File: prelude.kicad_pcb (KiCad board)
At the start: 2 copper layers, 80 x 60 mm, 35 parts, among them J1 CONN_01X50, J2 USB_C, J3 CONN_01X04, J4 CONN_01X08, SW1 SW_Push, U1 LM3671MF-3.3, U2 STM32F411RETx, U3 AP5724, Y1 16MHz

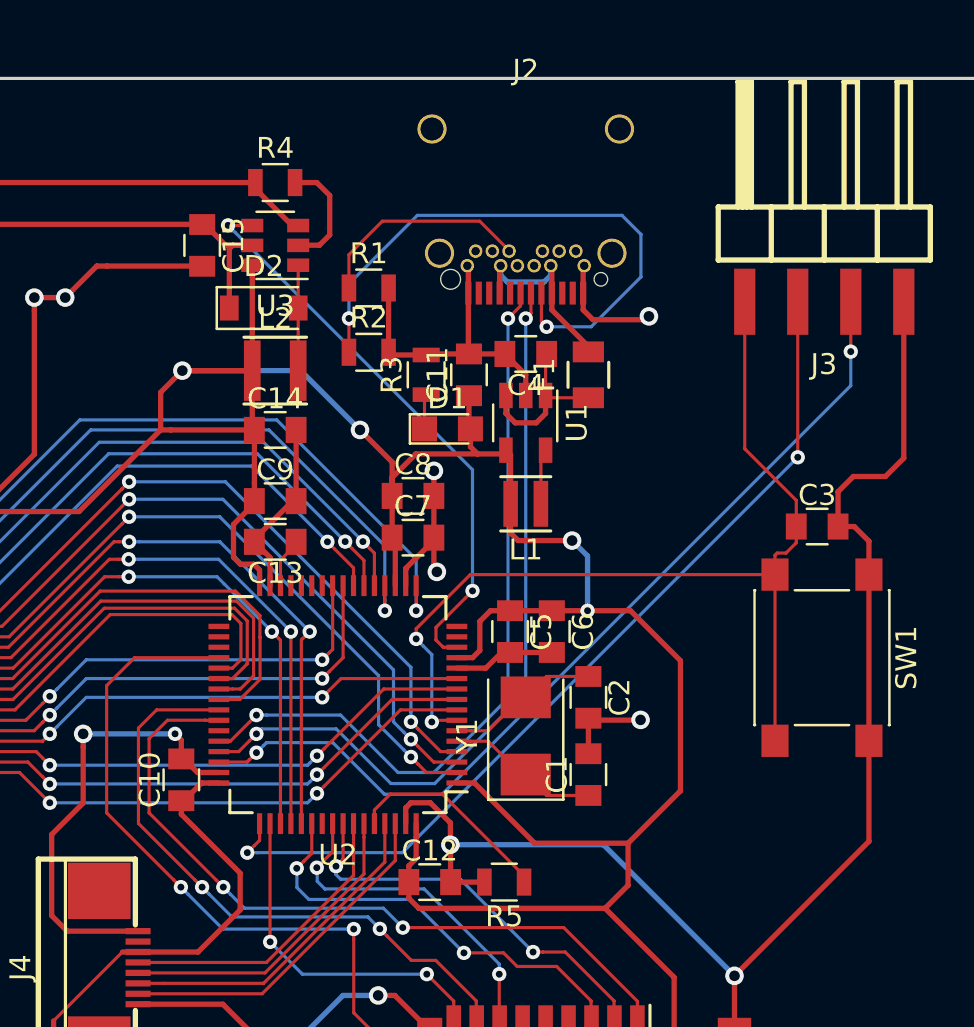
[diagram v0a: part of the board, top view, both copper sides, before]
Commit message: Updates to prelude.kicad_pcb
Reloaded updated netlist, exchanged footprints, adjusted J2 connector and rerouted USB-C portion.
Adds R6, which had not been imported before (by mistake)
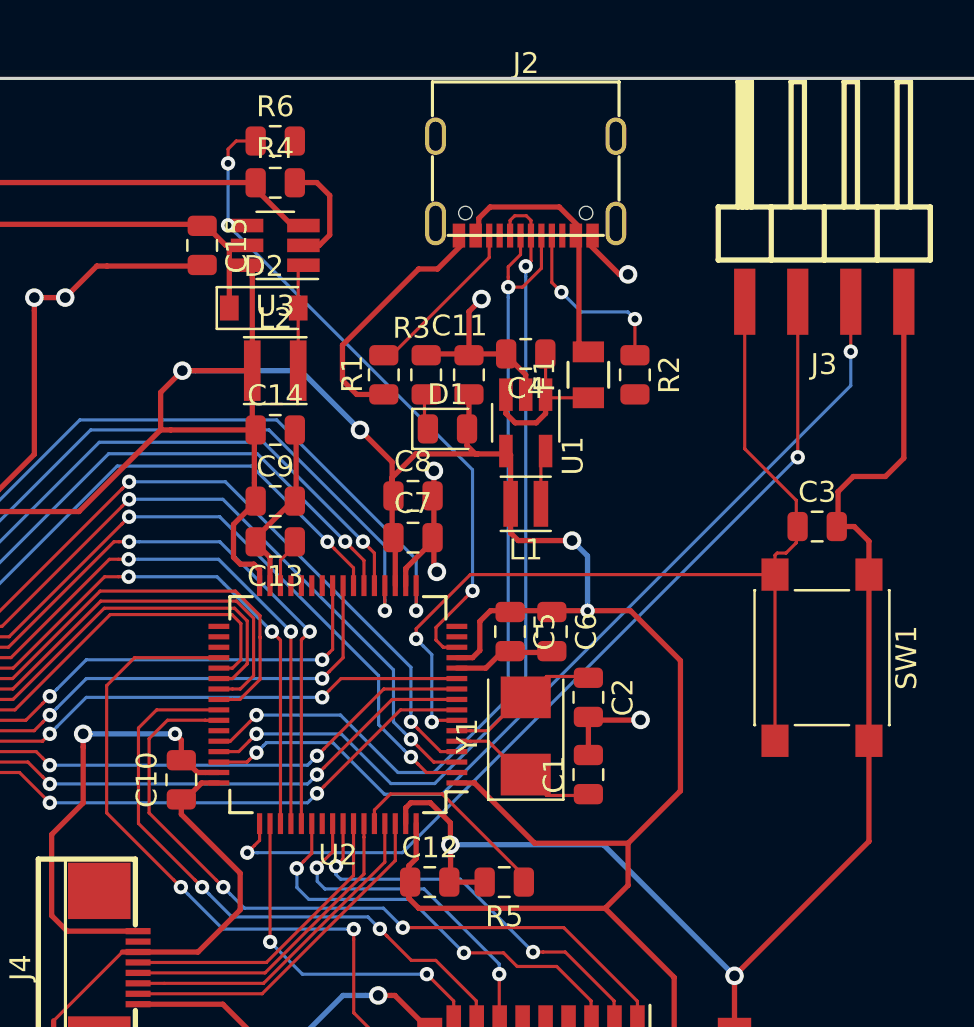
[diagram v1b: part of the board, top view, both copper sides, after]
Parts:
- added R6: 10K, Resistor_SMD:R_0805_2012Metric, F.Cu at (163.0, 43.0)
- C1, C10, C11, C12, C13, C14, C15, C2, C3, C4, C5, C6, C7, C8, C9: footprint Capacitors_SMD:C_0805 -> Capacitor_SMD:C_0805_2012Metric
- D1: footprint LEDs:LED_0805 -> LED_SMD:LED_0805_2012Metric
- D2: footprint Diodes_SMD:D_SOD-123 -> Diode_SMD:D_SOD-123
- J2: footprint volium:Amphenol_12401548E4#2A -> volium:D0-9062-005LG
- J3: value CONN_01X04 -> Conn_01x04
- J4: value CONN_01X08 -> Conn_01x08
- L1: footprint Inductors:Inductor_Taiyo-Yuden_NR-24xx -> Inductor_SMD:L_Taiyo-Yuden_NR-24xx
- L2: footprint Inductors:Inductor_Taiyo-Yuden_NR-30xx -> Inductor_SMD:L_Taiyo-Yuden_NR-30xx
- R1, R2, R3, R4, R5: footprint Resistors_SMD:R_0805 -> Resistor_SMD:R_0805_2012Metric
- SW1: footprint Buttons_Switches_SMD:SW_SPST_PTS645 -> Button_Switch_SMD:SW_SPST_PTS645
- U1: footprint TO_SOT_Packages_SMD:TSOT-23-5 -> Package_TO_SOT_SMD:SOT-23-5_HandSoldering
- U2: footprint Housings_QFP:LQFP-64_10x10mm_Pitch0.5mm -> Package_QFP:LQFP-64_10x10mm_P0.5mm
- U3: footprint TO_SOT_Packages_SMD:SOT-23-6 -> Package_TO_SOT_SMD:SOT-23-6_Handsoldering
- XS1: value SD_ebay-uSD-push/push_SMD -> SD_ebay-uSD-push_push_SMD
- Y1: footprint Crystals:Crystal_SMD_5032-2pin_5.0x3.2mm -> Crystal:Crystal_SMD_5032-2Pin_5.0x3.2mm
- moved R2 12.8 mm to (180.2, 54.2), turned to 270 degrees
- moved R1 4.22 mm to (168.2, 54.2), turned to 270 degrees
- moved J2 1.75 mm to (175.0, 43.9)
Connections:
- J1 pad 1: (no net) -> Net-(J1-Pad1)
- J1 pad 10: (no net) -> Net-(J1-Pad10)
- J1 pad 11: (no net) -> Net-(J1-Pad11)
- J1 pad 12: (no net) -> Net-(J1-Pad12)
- J1 pad 13: (no net) -> Net-(J1-Pad13)
- J1 pad 14: (no net) -> Net-(J1-Pad14)
- J1 pad 15: (no net) -> Net-(J1-Pad15)
- J1 pad 16: (no net) -> Net-(J1-Pad16)
- J1 pad 2: (no net) -> Net-(J1-Pad2)
- J1 pad 3: (no net) -> Net-(J1-Pad3)
- J1 pad 33: (no net) -> Net-(J1-Pad33)
- J1 pad 34: (no net) -> Net-(J1-Pad34)
- J1 pad 35: (no net) -> Net-(J1-Pad35)
- J1 pad 36: (no net) -> Net-(J1-Pad36)
- J1 pad 4: (no net) -> Net-(J1-Pad4)
- J1 pad 42: (no net) -> Net-(J1-Pad42)
- J1 pad 43: (no net) -> Net-(J1-Pad43)
- J1 pad 44: (no net) -> Net-(J1-Pad44)
- J1 pad 45: (no net) -> Net-(J1-Pad45)
- J1 pad 46: (no net) -> Net-(J1-Pad46)
- J1 pad 47: (no net) -> Net-(J1-Pad47)
- J1 pad 48: (no net) -> Net-(J1-Pad48)
- J1 pad 9: (no net) -> Net-(J1-Pad9)
- J2 pad A8: (no net) -> Net-(J2-PadA8)
- J2 pad B6: (no net) -> /USB_D+
- J2 pad B7: (no net) -> /USB_D-
- J2 pad B8: (no net) -> Net-(J2-PadB8)
- J4 pad 2: (no net) -> Net-(J4-Pad2)
- U2 pad 15: (no net) -> Net-(U2-Pad15)
- U2 pad 16: (no net) -> Net-(U2-Pad16)
- U2 pad 26: (no net) -> Net-(U2-Pad26)
- U2 pad 27: (no net) -> Net-(U2-Pad27)
- U2 pad 28: (no net) -> Net-(U2-Pad28)
- U2 pad 29: (no net) -> Net-(U2-Pad29)
- U2 pad 33: (no net) -> Net-(U2-Pad33)
- U2 pad 34: (no net) -> Net-(U2-Pad34)
- U2 pad 35: (no net) -> Net-(U2-Pad35)
- U2 pad 43: (no net) -> Net-(U2-Pad43)
- U2 pad 55: (no net) -> Net-(U2-Pad55)
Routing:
- net Net-(J2-PadA5): track 28.3 -> 8.69 mm
- net /USB_D-: track 36.6 -> 42.9 mm
- net /LED_CTRL: track 27.7 -> 33.1 mm, vias 2 -> 3
- net /USB_D+: track 37.3 -> 42.5 mm
- net GND: track 207.6 -> 211.3 mm, vias 12 -> 13
- net /VBUS: track 9.92 -> 13.0 mm
- net Net-(J2-PadB5): track 10.6 -> 8.04 mm

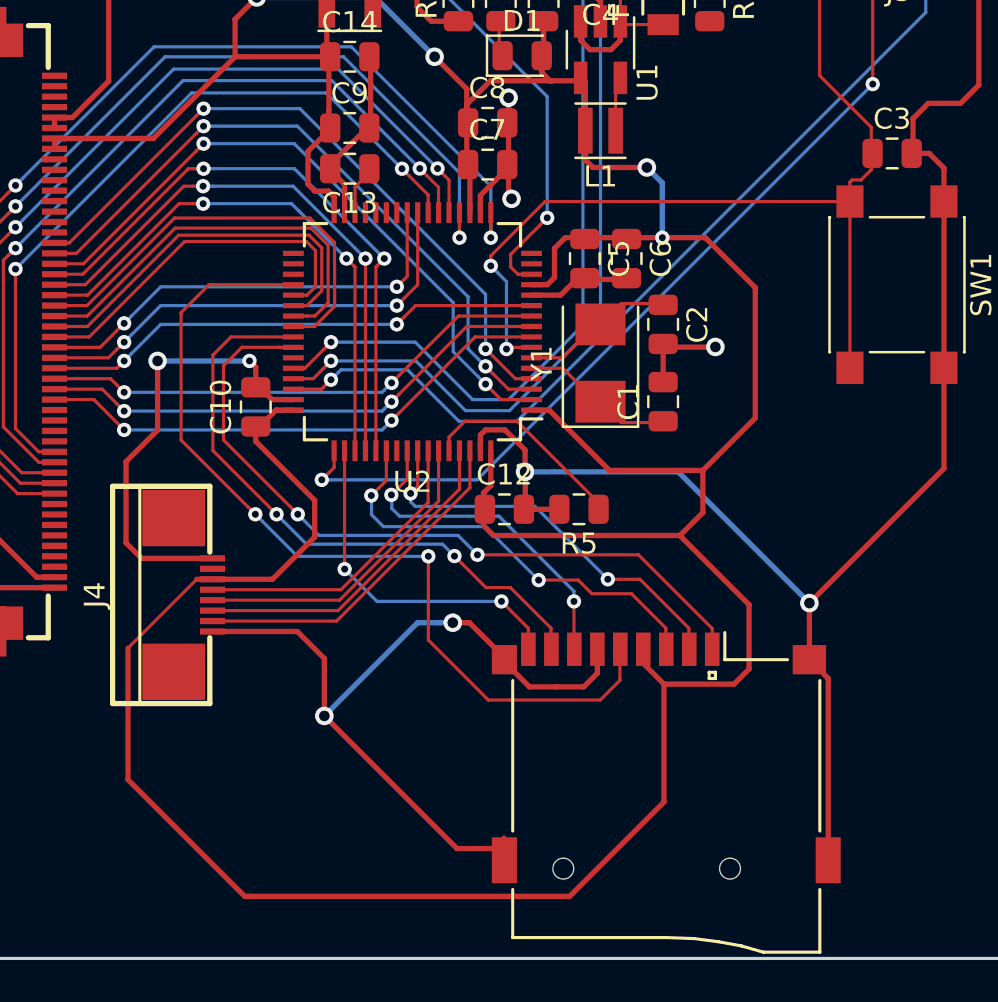
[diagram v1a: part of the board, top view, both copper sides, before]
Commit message: Fixes some routing issues
One pwr track was too narrow
Aligned vias for SDIO signals CMD, D0 and D3
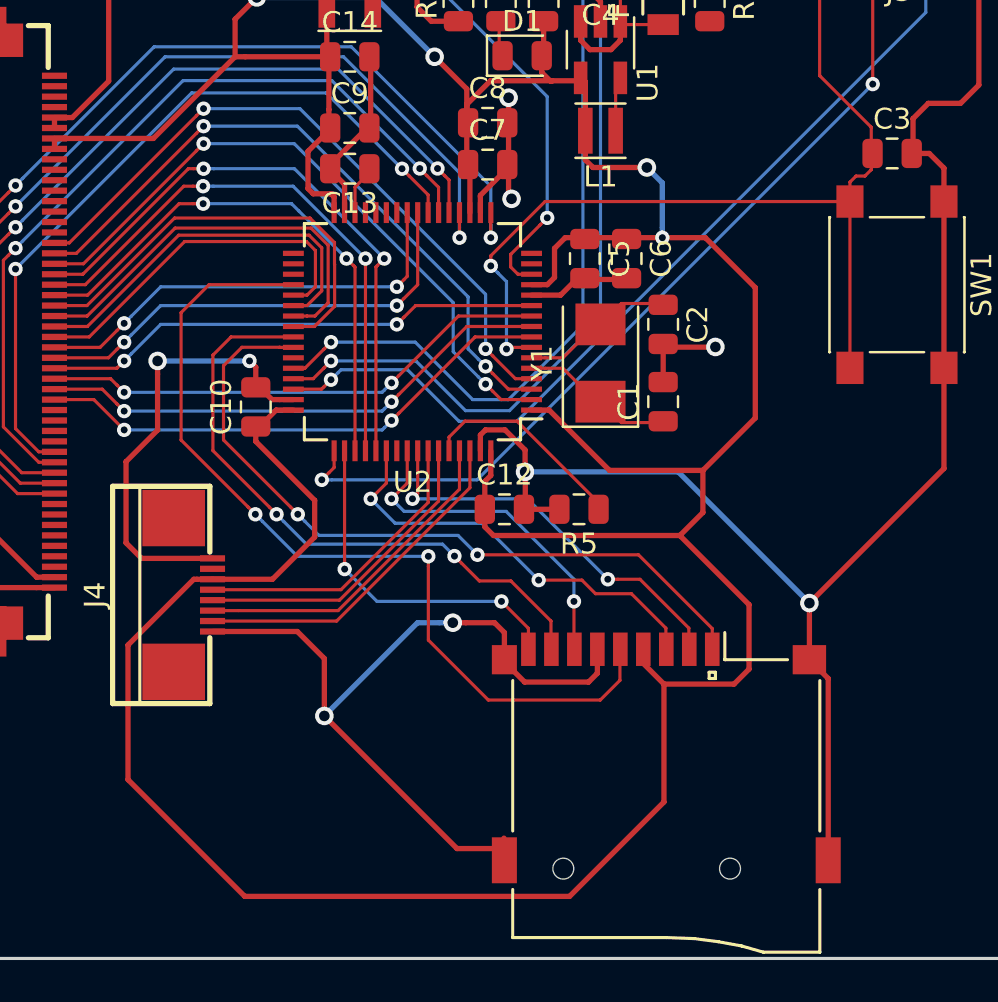
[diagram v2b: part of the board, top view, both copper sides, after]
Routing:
- net GND: track 211.3 -> 211.8 mm

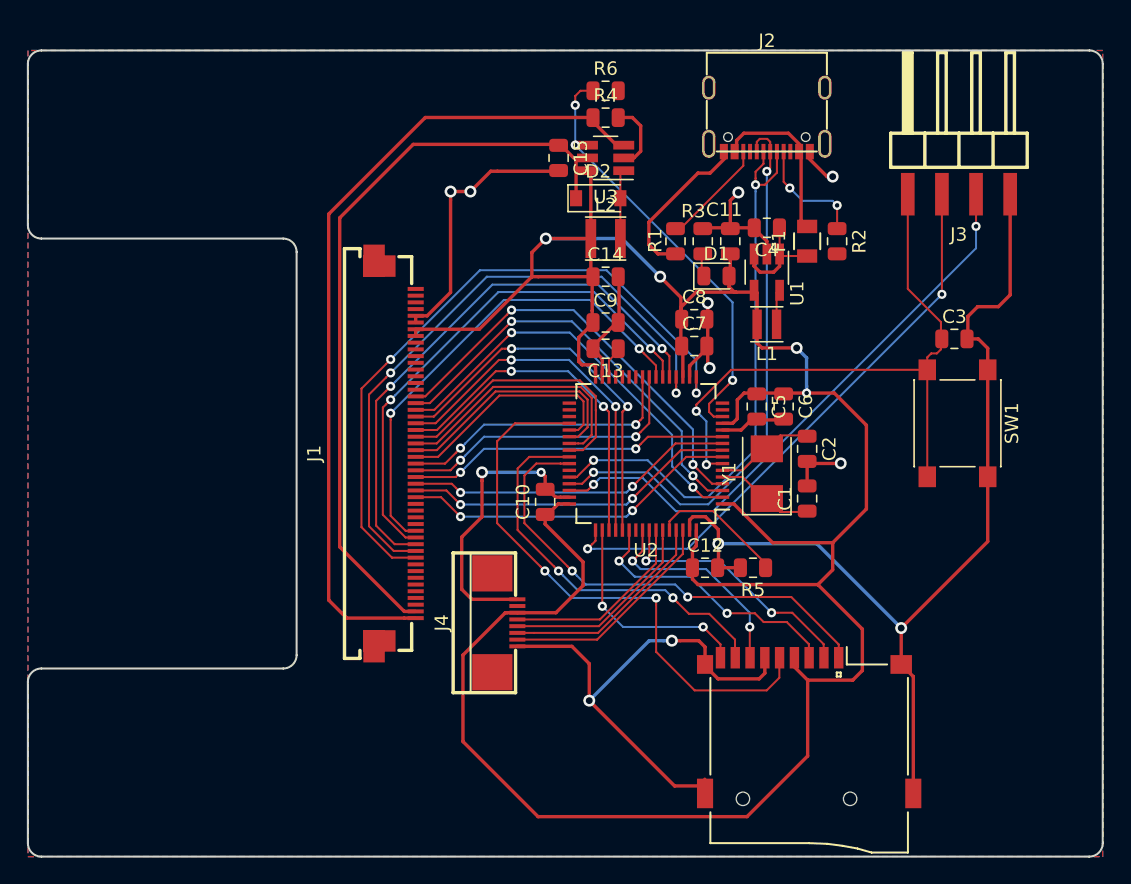
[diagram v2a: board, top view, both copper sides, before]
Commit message: Final touches to prelude
Added via stitching, fixed alignment issues, moved references in silkscreen, added OSH logo and project name and revision
Updates main prelude.pro project file
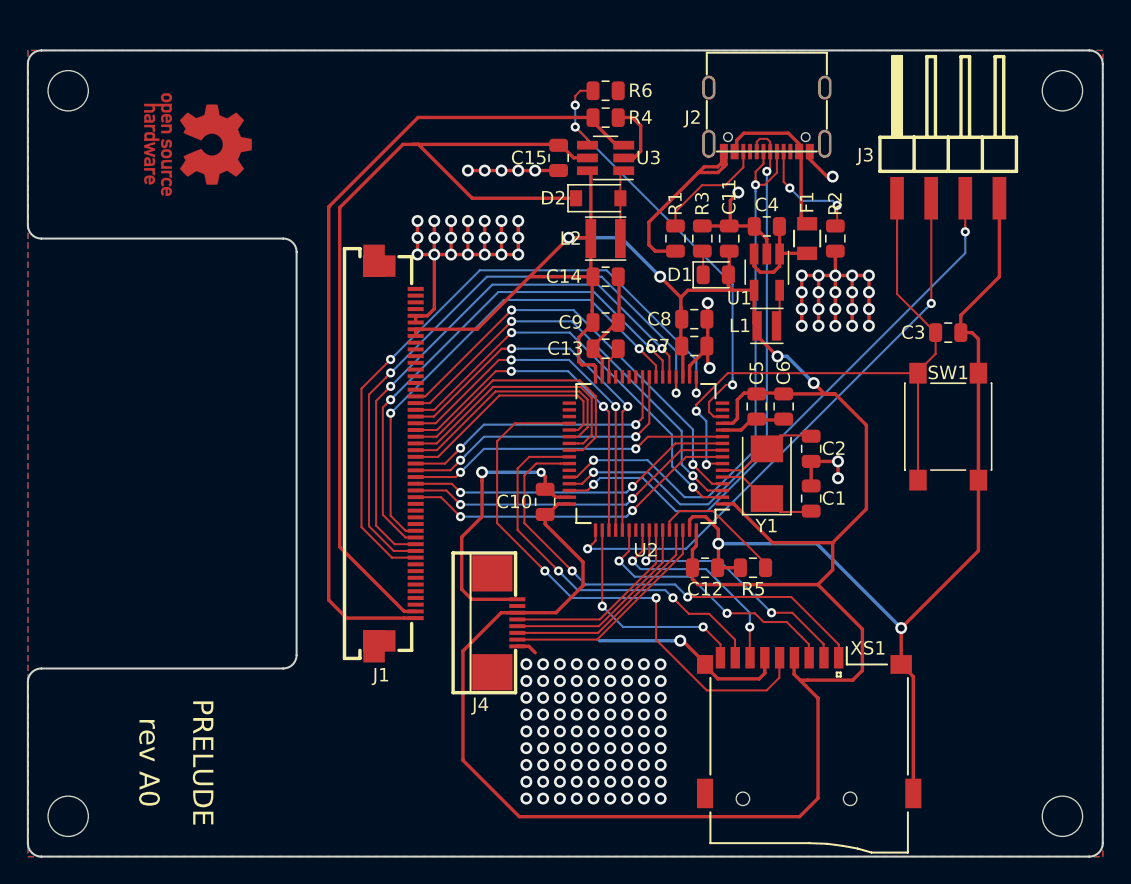
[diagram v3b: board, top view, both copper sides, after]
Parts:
- added REF**: OSHW-Logo_7.5x8mm_Copper, Symbol:OSHW-Logo_7.5x8mm_Copper, F.Cu at (132.7, 47.0)
- added REF**: MountingHole_3mm, MountingHole:MountingHole_3mm, F.Cu at (123.0, 43.0)
- added REF**: MountingHole_3mm, MountingHole:MountingHole_3mm, F.Cu at (123.0, 97.0)
- added REF**: MountingHole_3mm, MountingHole:MountingHole_3mm, F.Cu at (197.0, 97.0)
- added REF**: MountingHole_3mm, MountingHole:MountingHole_3mm, F.Cu at (197.0, 43.0)
- moved J3 0.85 mm to (188.5, 51.0)
- moved SW1 0.73 mm to (188.5, 68.0)
- moved C3 0.66 mm to (188.5, 61.0)
- moved C1 0.30 mm to (178.3, 73.3)
- moved C2 0.30 mm to (178.3, 69.7)
- moved R2 0.24 mm to (180.1, 54.0)
- moved C11 0.22 mm to (172.2, 54.0)
- moved R3 0.20 mm to (170.2, 54.0)
- moved F1 0.20 mm to (178.0, 54.0)
- moved R1 0.20 mm to (168.2, 54.0)
- moved L1 0.12 mm to (175.0, 60.5)
- moved D1 0.10 mm to (171.2, 56.7)
- moved C4 0.10 mm to (175.0, 53.1)
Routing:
- net GND: track 211.8 -> 236.6 mm, vias 13 -> 138
- net /LED_A: track 56.6 -> 67.7 mm
- net /NRST: track 47.0 -> 50.4 mm
- net +3V3: track 204.8 -> 206.7 mm
- net Net-(J2-PadB5): track 8.04 -> 9.01 mm
- net /SWDIO: track 43.8 -> 42.9 mm
- net /LED_CTRL: track 33.1 -> 33.8 mm
- net /SWCLK: track 43.3 -> 42.6 mm
- net /SDIO_CLK: track 43.0 -> 42.4 mm
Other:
- rule pad_to_mask_clearance: 0.2 -> 0.0508
- board text added: "PRELUDE"
- board text added: "rev A0"

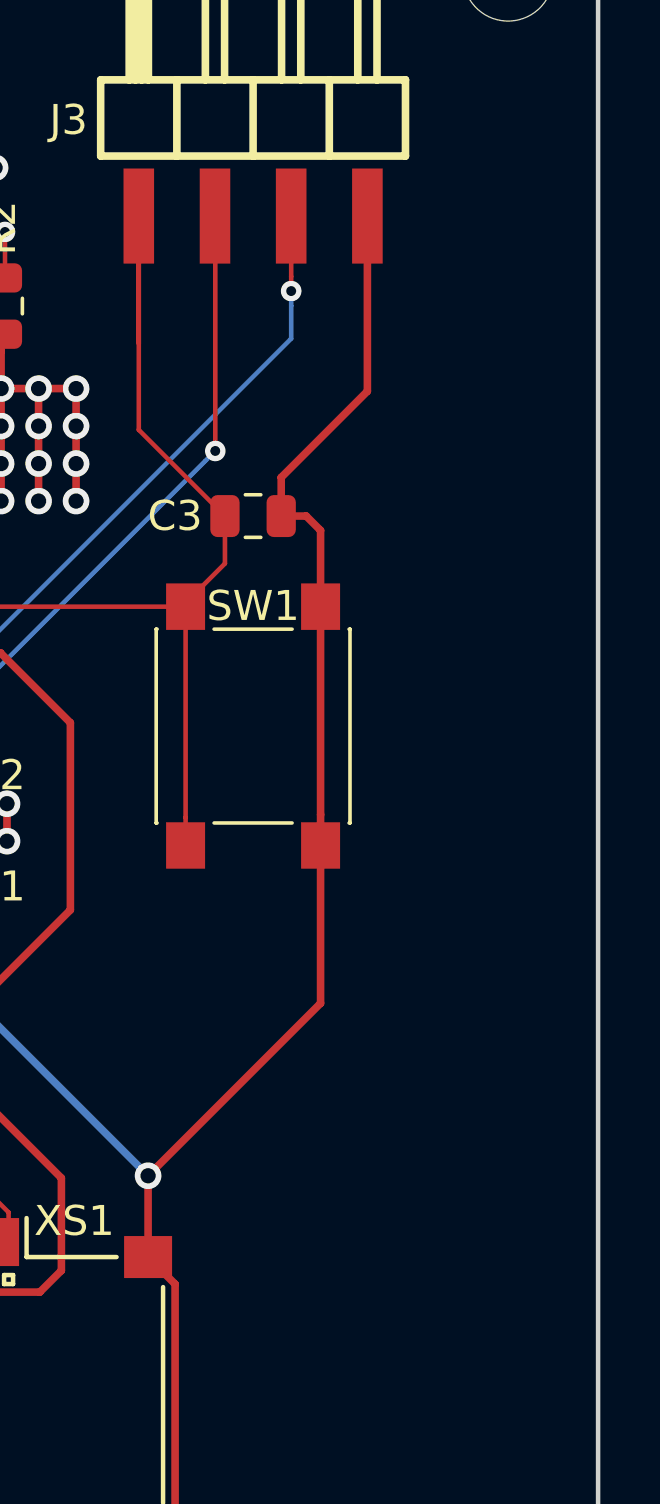
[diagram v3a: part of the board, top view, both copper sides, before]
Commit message: Adds more via stitching at the top of the board
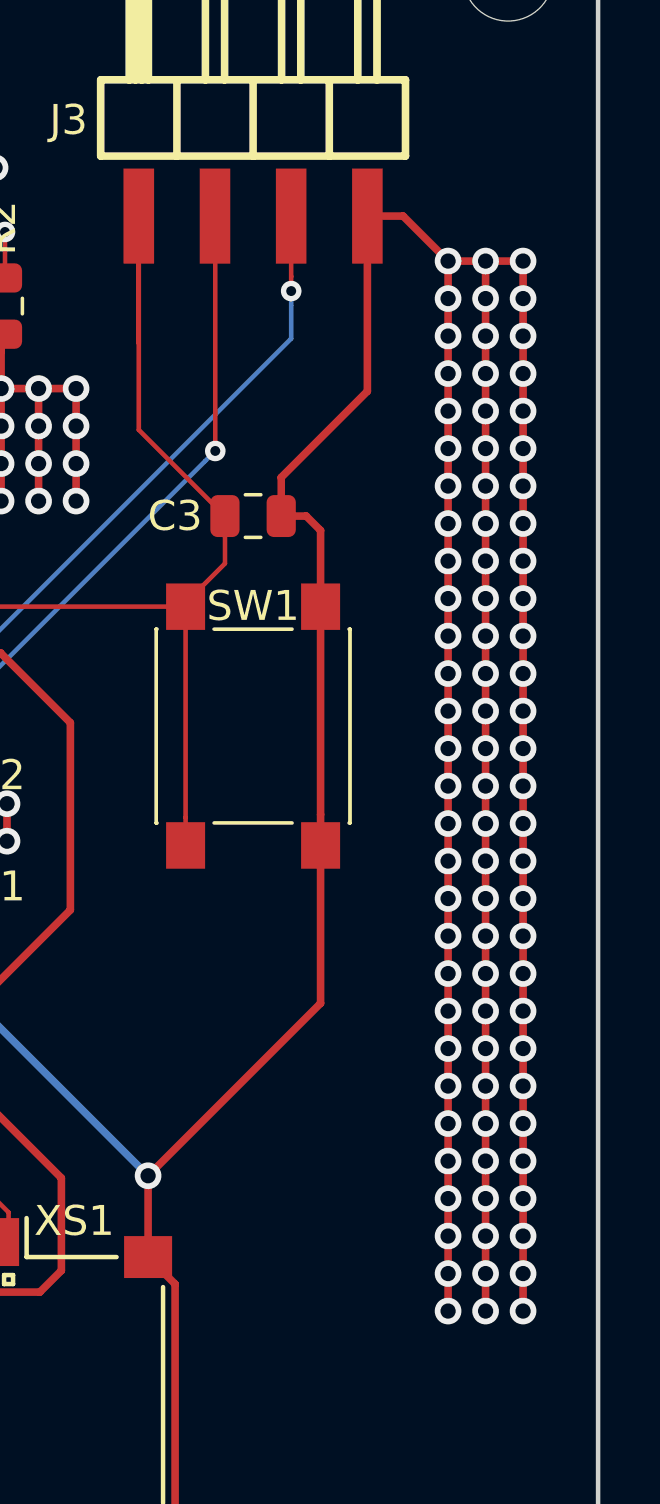
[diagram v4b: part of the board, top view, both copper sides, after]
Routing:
- net GND: track 236.6 -> 348.4 mm, vias 138 -> 225
